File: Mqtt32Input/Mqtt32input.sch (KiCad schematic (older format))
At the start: 42 parts, among them J1 INPUT 0-7, J10 SLAVE2 IN/DATA OUTPUT, J2 JP OPT1, J3 JP OPT2, J4 INPUT 8-15, J5 INPUT 16-23, J6 SLAVE1IN/CHAIN INPUT, J7 JP CHAIN IN(1)/SLAVE1(3), J8 JP DATA OUT(1)/SLAVE2(3), J9 INPUT 24-31, SW1 DIP NODE 0-3, SW2 DIP # Chain length, U1 74HC165, U2 74HC165, U3 74HC165, U4 74HC165, X1 0V - 5V

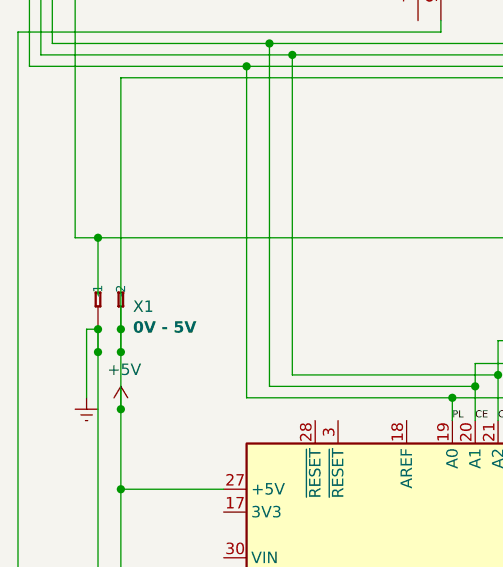
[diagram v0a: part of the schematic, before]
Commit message: Fix component placement, and GND connexion + board size on inputs
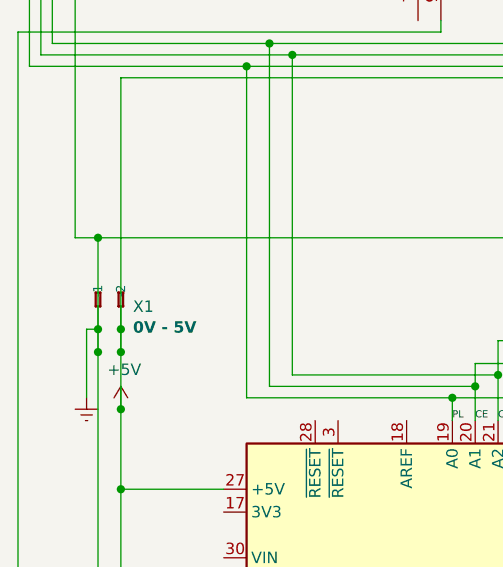
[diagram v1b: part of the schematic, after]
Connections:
- net Earth: now also R11.2, RN1.1 (common), RN10.1 (common), RN4.1 (common), RN7.1 (common), U1.8 (GND), U2.8 (GND), U3.8 (GND), U4.8 (GND)
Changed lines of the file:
@@
 Connection ~ 3100 3550
-Wire Wire Line
-	1300 4500 1300 4250
 Wire Wire Line
 	1300 4250 3850 4250
@@
 Wire Wire Line
 	10550 5050 10550 6350
+Wire Wire Line
+	1300 4250 1300 4650
 $EndSCHEMATC

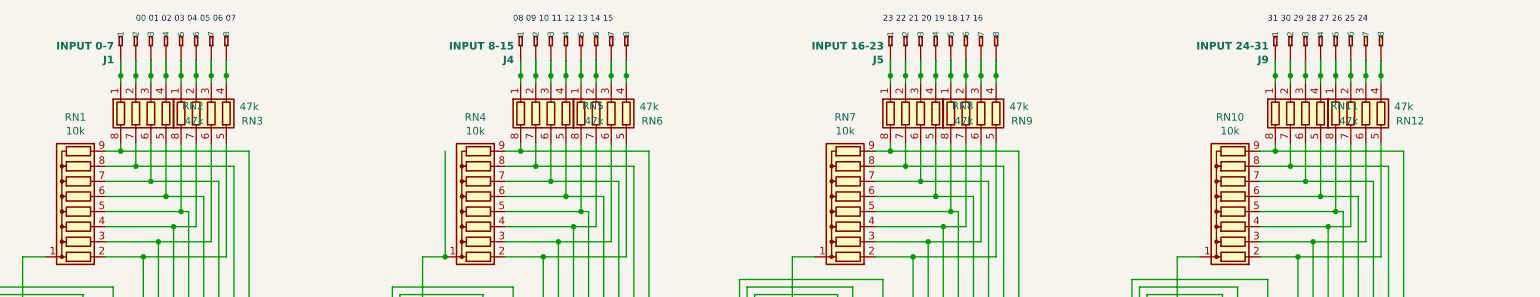
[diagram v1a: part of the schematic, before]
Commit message: Revision with through hole resistor, more robust that SMD Array
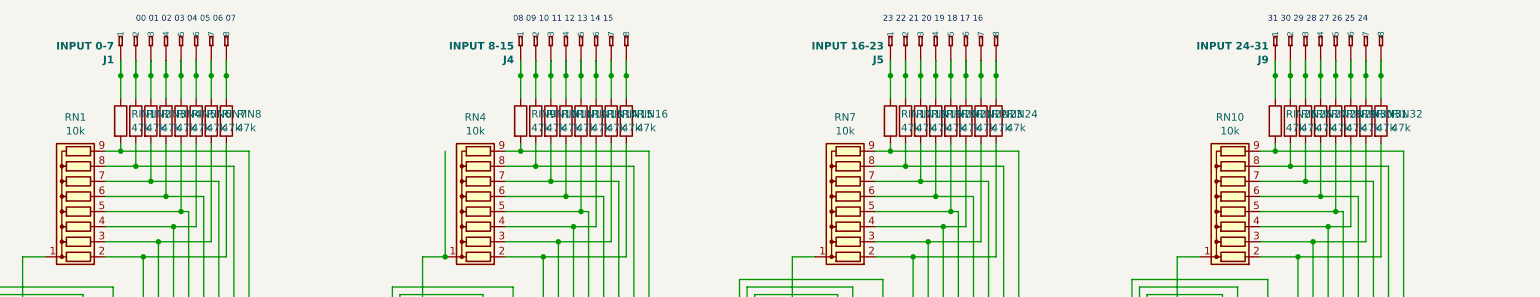
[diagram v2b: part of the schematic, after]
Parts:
- removed RN11, RN12, RN2, RN3, RN5, RN6, RN8, RN9: 47k, _Extra_footprints:RESCAXS127P508X320X70-8N, symbol Device:R_Pack04
- added RIN1, RIN10, RIN11, RIN12, RIN13, RIN14, RIN15, RIN16, RIN17, RIN18, RIN19, RIN2, RIN20, RIN21, RIN22, RIN23, RIN24, RIN25, RIN26, RIN27, RIN28, RIN29, RIN3, RIN30, RIN31, RIN32, RIN4, RIN5, RIN6, RIN7, RIN8, RIN9: 47k, Resistor_THT:R_Axial_DIN0207_L6.3mm_D2.5mm_P2.54mm_Vertical, symbol Device:R
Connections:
- net at RN1.9 (R8), U1.11 (D0): now also RIN1.2
- net at RN1.8 (R7), U1.12 (D1): now also RIN2.2
- net at RN1.7 (R6), U1.13 (D2): now also RIN3.2
- net at RN1.6 (R5), U1.14 (D3): now also RIN4.2
- net at RN1.5 (R4), U1.3 (D4): now also RIN5.2
- net at RN1.4 (R3), U1.4 (D5): now also RIN6.2
- net at RN1.3 (R2), U1.5 (D6): now also RIN7.2
- net at RN1.2 (R1), U1.6 (D7): now also RIN8.2
- net at J1.A1 (-1), J1.B1: now also RIN1.1
- net at J1.A2 (-2), J1.B2: now also RIN2.1
- net at J1.A3 (-3), J1.B3: now also RIN3.1
- net at J1.A4 (-4), J1.B4: now also RIN4.1
- net at J1.A5 (-5), J1.B5: now also RIN5.1
- net at J1.A6 (-6), J1.B6: now also RIN6.1
- net at J1.A7 (-7), J1.B7: now also RIN7.1
- net at J1.A8 (-8), J1.B8: now also RIN8.1
- net at J4.A1 (-1), J4.B1: now also RIN9.1
- net at J4.A2 (-2), J4.B2: now also RIN10.1
- net at J4.A3 (-3), J4.B3: now also RIN11.1
- net at J4.A4 (-4), J4.B4: now also RIN12.1
- net at J4.A5 (-5), J4.B5: now also RIN13.1
- net at J4.A6 (-6), J4.B6: now also RIN14.1
- net at J4.A7 (-7), J4.B7: now also RIN15.1
- net at J4.A8 (-8), J4.B8: now also RIN16.1
- net at RN4.9 (R8), U2.11 (D0): now also RIN9.2
- net at RN4.8 (R7), U2.12 (D1): now also RIN10.2
- net at RN4.7 (R6), U2.13 (D2): now also RIN11.2
- net at RN4.6 (R5), U2.14 (D3): now also RIN12.2
- net at RN4.5 (R4), U2.3 (D4): now also RIN13.2
- net at RN4.4 (R3), U2.4 (D5): now also RIN14.2
- net at RN4.3 (R2), U2.5 (D6): now also RIN15.2
- net at RN4.2 (R1), U2.6 (D7): now also RIN16.2
- net at J5.A1 (-1), J5.B1: now also RIN17.1
- net at J5.A2 (-2), J5.B2: now also RIN18.1
- net at J5.A3 (-3), J5.B3: now also RIN19.1
- net at J5.A4 (-4), J5.B4: now also RIN20.1
- net at J5.A5 (-5), J5.B5: now also RIN21.1
- net at J5.A6 (-6), J5.B6: now also RIN22.1
- net at J5.A7 (-7), J5.B7: now also RIN23.1
- net at J5.A8 (-8), J5.B8: now also RIN24.1
- net at RN7.9 (R8), U3.11 (D0): now also RIN17.2
- net at RN7.8 (R7), U3.12 (D1): now also RIN18.2
- net at RN7.7 (R6), U3.13 (D2): now also RIN19.2
- net at RN7.6 (R5), U3.14 (D3): now also RIN20.2
- net at RN7.5 (R4), U3.3 (D4): now also RIN21.2
- net at RN7.4 (R3), U3.4 (D5): now also RIN22.2
- net at RN7.3 (R2), U3.5 (D6): now also RIN23.2
- net at RN7.2 (R1), U3.6 (D7): now also RIN24.2
- net at J9.A1 (-1), J9.B1: now also RIN25.1
- net at J9.A2 (-2), J9.B2: now also RIN26.1
- net at J9.A3 (-3), J9.B3: now also RIN27.1
- net at J9.A4 (-4), J9.B4: now also RIN28.1
- net at J9.A5 (-5), J9.B5: now also RIN29.1
- net at J9.A6 (-6), J9.B6: now also RIN30.1
- net at J9.A7 (-7), J9.B7: now also RIN31.1
- net at J9.A8 (-8), J9.B8: now also RIN32.1
- net at RN10.9 (R8), U4.11 (D0): now also RIN25.2
- net at RN10.8 (R7), U4.12 (D1): now also RIN26.2
- net at RN10.7 (R6), U4.13 (D2): now also RIN27.2
- net at RN10.6 (R5), U4.14 (D3): now also RIN28.2
- net at RN10.5 (R4), U4.3 (D4): now also RIN29.2
- net at RN10.4 (R3), U4.4 (D5): now also RIN30.2
- net at RN10.3 (R2), U4.5 (D6): now also RIN31.2
- net at RN10.2 (R1), U4.6 (D7): now also RIN32.2
